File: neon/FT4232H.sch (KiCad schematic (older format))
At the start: 1 part

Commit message: Add all hierarchical pins
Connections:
- net DD7: now reaches U?.31 (DD7)
- net DD5: now reaches U?.32 (DD5)
- net DD4: now reaches U?.33 (DD4)
- net DD2: now reaches U?.34 (DD2)
- net DD0: now reaches U?.35 (DD0)
- net CD6: now reaches U?.36 (CD6)
- net CD4: now reaches U?.37 (CD4)
- net CD3: now reaches U?.38 (CD3)
- net CD1: now reaches U?.39 (CD1)
- net DD6: now reaches U?.44 (DD6)
- net DD3: now reaches U?.46 (DD3)
- net DD1: now reaches U?.47 (DD1)
- net CD7: now reaches U?.48 (CD7)
- net CD5: now reaches U?.49 (CD5)
- net CD2: now reaches U?.51 (CD2)
- net CD0: now reaches U?.52 (CD0)
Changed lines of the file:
@@
 Wire Wire Line
 	5950 3600 5900 3600
+Text HLabel 5900 3700 0    50   UnSpc ~ 0
+BD0
+Text HLabel 5900 3800 0    50   UnSpc ~ 0
+BD2
+Text HLabel 5900 3900 0    50   UnSpc ~ 0
+BD4
+Text HLabel 5900 4000 0    50   UnSpc ~ 0
+BD5
+Text HLabel 5900 4100 0    50   UnSpc ~ 0
+BD7
+Text HLabel 7150 3700 2    50   UnSpc ~ 0
+BD1
+Text HLabel 7150 3800 2    50   UnSpc ~ 0
+BD3
+Text HLabel 7150 4000 2    50   UnSpc ~ 0
+BD6
+Text HLabel 5400 3300 2    50   UnSpc ~ 0
+DD7
+Text HLabel 5400 3400 2    50   UnSpc ~ 0
+DD5
+Text HLabel 5400 3500 2    50   UnSpc ~ 0
+DD4
+Text HLabel 5400 3600 2    50   UnSpc ~ 0
+DD2
+Text HLabel 5400 3700 2    50   UnSpc ~ 0
+DD0
+Text HLabel 5400 3800 2    50   UnSpc ~ 0
+CD6
+Text HLabel 5400 3900 2    50   UnSpc ~ 0
+CD4
+Text HLabel 5400 4000 2    50   UnSpc ~ 0
+CD3
+Text HLabel 5400 4100 2    50   UnSpc ~ 0
+CD1
+Text HLabel 4150 4100 0    50   UnSpc ~ 0
+CD0
+Text HLabel 4150 4000 0    50   UnSpc ~ 0
+CD2
+Text HLabel 4150 3800 0    50   UnSpc ~ 0
+CD5
+Text HLabel 4150 3700 0    50   UnSpc ~ 0
+CD7
+Text HLabel 4150 3600 0    50   UnSpc ~ 0
+DD1
+Text HLabel 4150 3500 0    50   UnSpc ~ 0
+DD3
+Text HLabel 4150 3300 0    50   UnSpc ~ 0
+DD6
+Wire Wire Line
+	5400 3300 5350 3300
+Wire Wire Line
+	5400 3400 5350 3400
+Wire Wire Line
+	5400 3500 5350 3500
+Wire Wire Line
+	5400 3600 5350 3600
+Wire Wire Line
+	5400 3700 5350 3700
+Wire Wire Line
+	5400 3800 5350 3800
+Wire Wire Line
+	5400 3900 5350 3900
+Wire Wire Line
+	5400 4000 5350 4000
+Wire Wire Line
+	5400 4100 5350 4100
+Wire Wire Line
+	4150 4100 4200 4100
+Wire Wire Line
+	4150 4000 4200 4000
+Wire Wire Line
+	4200 3800 4150 3800
+Wire Wire Line
+	4200 3700 4150 3700
+Wire Wire Line
+	4200 3600 4150 3600
+Wire Wire Line
+	4200 3500 4150 3500
+Wire Wire Line
+	4200 3300 4150 3300
 $EndSCHEMATC

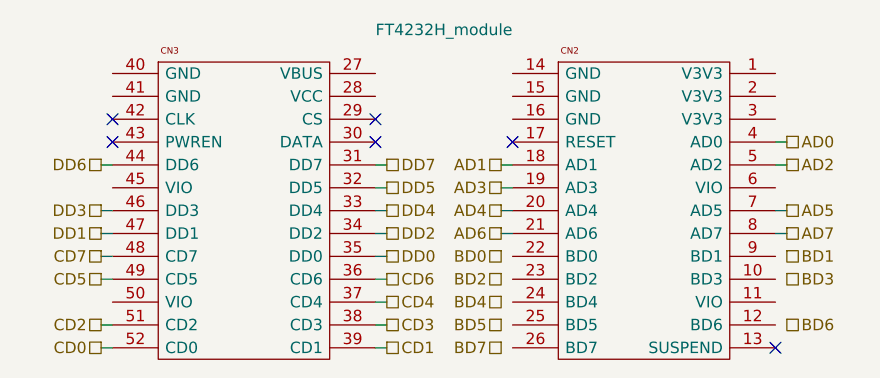
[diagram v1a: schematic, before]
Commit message: Add more hierarchical pins
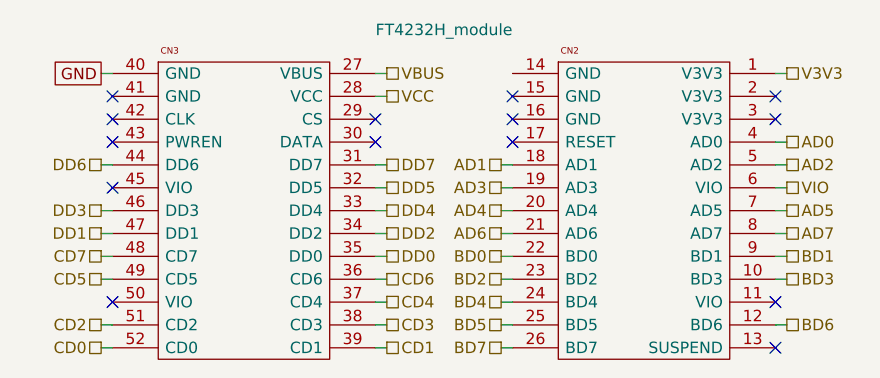
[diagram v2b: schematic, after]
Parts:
- gave numbers to parts that had none: 1
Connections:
- net BD0: now also U1.22 (BD0)
- net BD1: now also U1.9 (BD1)
- net BD2: now also U1.23 (BD2)
- net BD3: now also U1.10 (BD3)
- net BD4: now also U1.24 (BD4)
- net BD5: now also U1.25 (BD5)
- net BD6: now also U1.12 (BD6)
- net BD7: now also U1.26 (BD7)
- net V3V3: now reaches U1.1 (V3V3)
- net VBUS: now reaches U1.27 (VBUS)
- net VCC: now reaches U1.28 (VCC)
- net GND: now reaches U1.40 (GND)
- net VIO: now reaches U1.6 (VIO)
- no-connect marks 6 -> 14
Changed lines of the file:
@@
 Text HLabel 5900 3500 0    50   UnSpc ~ 0
 AD4
-$Comp
-L FTDI:FT4232H_module U?
-U 1 1 5F4CD349
-P 5900 2900
-F 0 "U?" H 4400 3200 50  0001 L CNN
-F 1 "FT4232H_module" H 5650 3091 50  0000 C CNN
-F 2 "" H 6950 3000 50  0001 L CNN
-F 3 "" H 6950 2900 50  0001 L CNN
-	1    5900 2900
-	1    0    0    -1
-$EndComp
 Wire Wire Line
 	7150 3200 7100 3200
@@
 Wire Wire Line
 	4200 3300 4150 3300
+Wire Wire Line
+	7150 4000 7100 4000
+Wire Wire Line
+	7150 3800 7100 3800
+Wire Wire Line
+	7150 3700 7100 3700
+Text HLabel 7150 2900 2    50   UnSpc ~ 0
+V3V3
+Wire Wire Line
+	7150 2900 7100 2900
+NoConn ~ 7100 3000
+NoConn ~ 7100 3100
+Text HLabel 7150 3400 2    50   UnSpc ~ 0
+VIO
+Wire Wire Line
+	7150 3400 7100 3400
+NoConn ~ 7100 3900
+Text HLabel 5400 2900 2    50   UnSpc ~ 0
+VBUS
+Text HLabel 5400 3000 2    50   UnSpc ~ 0
+VCC
+Wire Wire Line
+	5400 2900 5350 2900
+Wire Wire Line
+	5400 3000 5350 3000
+NoConn ~ 5950 3100
+NoConn ~ 5950 3000
+NoConn ~ 4200 3000
+NoConn ~ 4200 3900
+NoConn ~ 4200 3400
+Wire Wire Line
+	5950 3700 5900 3700
+Wire Wire Line
+	5950 3800 5900 3800
+Wire Wire Line
+	5950 3900 5900 3900
+Wire Wire Line
+	5950 4000 5900 4000
+Wire Wire Line
+	5950 4100 5900 4100
+Text GLabel 4150 2900 0    50   UnSpc ~ 0
+GND
+$Comp
+L FTDI:FT4232H_module U1
+U 1 1 5F4CD349
+P 5900 2900
+F 0 "U1" H 4400 3200 50  0001 L CNN
+F 1 "FT4232H_module" H 5650 3091 50  0000 C CNN
+F 2 "" H 6950 3000 50  0001 L CNN
+F 3 "" H 6950 2900 50  0001 L CNN
+	1    5900 2900
+	1    0    0    -1
+$EndComp
+Wire Wire Line
+	4200 2900 4150 2900
 $EndSCHEMATC

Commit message: Add LEDs
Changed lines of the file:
@@
 Wire Wire Line
 	7150 3700 7100 3700
-Text HLabel 7150 2900 2    50   UnSpc ~ 0
-V3V3
 Wire Wire Line
 	7150 2900 7100 2900
@@
 Wire Wire Line
 	4200 2900 4150 2900
+Text GLabel 7150 2900 2    50   Input ~ 0
+V3V3
 $EndSCHEMATC

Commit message: Assign footprints - part 1 and buggy
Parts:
- U1: footprint (none) -> neon_footprints:FT4232H-MINI-MODULE
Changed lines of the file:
@@
 F 0 "U1" H 4400 3200 50  0001 L CNN
 F 1 "FT4232H_module" H 5650 3091 50  0000 C CNN
-F 2 "" H 6950 3000 50  0001 L CNN
+F 2 "neon_footprints:FT4232H-MINI-MODULE" H 6950 3000 50  0001 L CNN
 F 3 "" H 6950 2900 50  0001 L CNN
 	1    5900 2900

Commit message: Pin warning fixes
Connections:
- no-connect marks 14 -> 15
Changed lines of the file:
@@
 Wire Wire Line
 	5950 4100 5900 4100
-Text GLabel 4150 2900 0    50   UnSpc ~ 0
-GND
 $Comp
 L FTDI:FT4232H_module U1
@@
 Text GLabel 7150 2900 2    50   Input ~ 0
 V3V3
+NoConn ~ 5950 2900
+$Comp
+L power:GND #PWR0101
+U 1 1 5F616FEF
+P 4150 2900
+F 0 "#PWR0101" H 4150 2650 50  0001 C CNN
+F 1 "GND" V 4155 2772 50  0000 R CNN
+F 2 "" H 4150 2900 50  0001 C CNN
+F 3 "" H 4150 2900 50  0001 C CNN
+	1    4150 2900
+	0    1    1    0
+$EndComp
 $EndSCHEMATC

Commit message: Version with shift register - schematic
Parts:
- U1: footprint neon_footprints:FT4232H-MINI-MODULE -> neon_footprints:FT4232H-MINI-MODULE-2
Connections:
- net CS: now reaches U1.29 (CS)
- net DATA: now reaches U1.30 (DATA)
- net CLK: now reaches U1.42 (CLK)
- net PWREN: now reaches U1.43 (PWREN)
- no-connect marks 15 -> 11
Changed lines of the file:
@@
 NoConn ~ 7100 4100
 NoConn ~ 5950 3200
-NoConn ~ 5350 3100
-NoConn ~ 5350 3200
-NoConn ~ 4200 3200
-NoConn ~ 4200 3100
 Text HLabel 7150 3300 2    50   UnSpc ~ 0
 AD2
@@
 F 0 "U1" H 4400 3200 50  0001 L CNN
 F 1 "FT4232H_module" H 5650 3091 50  0000 C CNN
-F 2 "neon_footprints:FT4232H-MINI-MODULE" H 6950 3000 50  0001 L CNN
+F 2 "neon_footprints:FT4232H-MINI-MODULE-2" H 6950 3000 50  0001 L CNN
 F 3 "" H 6950 2900 50  0001 L CNN
 	1    5900 2900
@@
 	0    1    1    0
 $EndComp
+Text HLabel 5400 3100 2    50   UnSpc ~ 0
+CS
+Text HLabel 5400 3200 2    50   UnSpc ~ 0
+DATA
+Wire Wire Line
+	5400 3100 5350 3100
+Wire Wire Line
+	5400 3200 5350 3200
+Text HLabel 4150 3100 0    50   UnSpc ~ 0
+CLK
+Text HLabel 4150 3200 0    50   UnSpc ~ 0
+PWREN
+Wire Wire Line
+	4200 3100 4150 3100
+Wire Wire Line
+	4200 3200 4150 3200
 $EndSCHEMATC
